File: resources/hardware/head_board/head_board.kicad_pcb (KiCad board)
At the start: 2 copper layers, 66 x 61 mm, 18 parts, among them IC1 ATMEGA328P-P, P1 SERIAL/RST, P2 PI_CONN, P3 REED, P4 PR, P5 CAM_LEDS, P6 STEPPER, P7 PR_LED, P8 FDBK_LED, U1 ULN2003

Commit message: added letterbox-setup.py
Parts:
- C1: value CP1 -> 10 uF
- R1: value R -> 56 Ohm
- R2: value R -> 10 kOhm
- R5, R6: value R -> 100 Ohm
- moved C1 1.65 mm to (149.5, 153.0)
- moved R2 1.27 mm to (163.5, 153.5)
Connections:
- IC1 pad 2: /PIRX -> /PITX
- IC1 pad 3: /PITX -> /PIRX
- P1 pad 2: /PIRX -> /PITX
- P1 pad 3: /PITX -> /PIRX
- R2 pad 2: Net-(C1-Pad2) -> /RST
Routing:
- net /RST: track 8.15 -> 15.5 mm
- net Net-(C1-Pad2): track 11.1 -> 5.62 mm
- net /PITX: track 140.0 -> 144.4 mm, vias 3 -> 1
- net /PIRX: track 139.7 -> 138.7 mm, vias 1 -> 3
- net +3V3: track 95.7 -> 96.5 mm

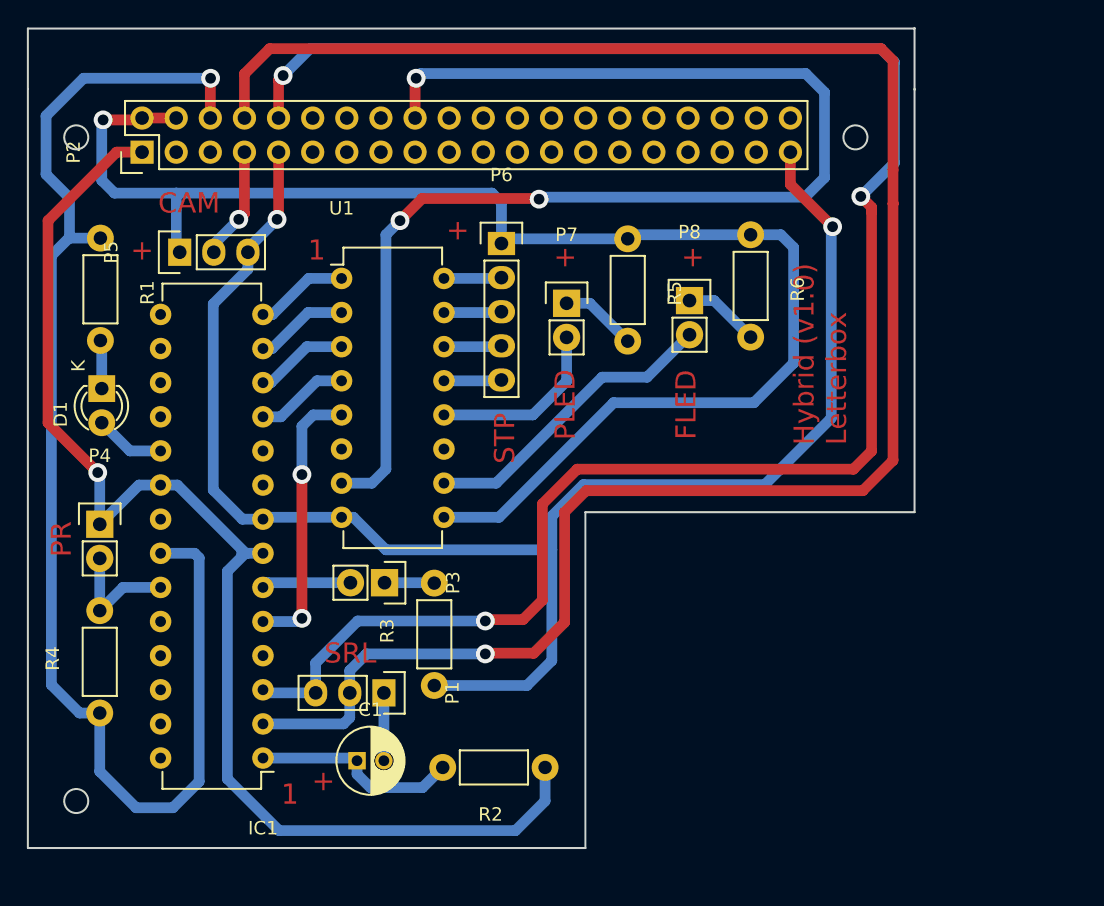
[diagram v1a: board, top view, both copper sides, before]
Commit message: added stepper board
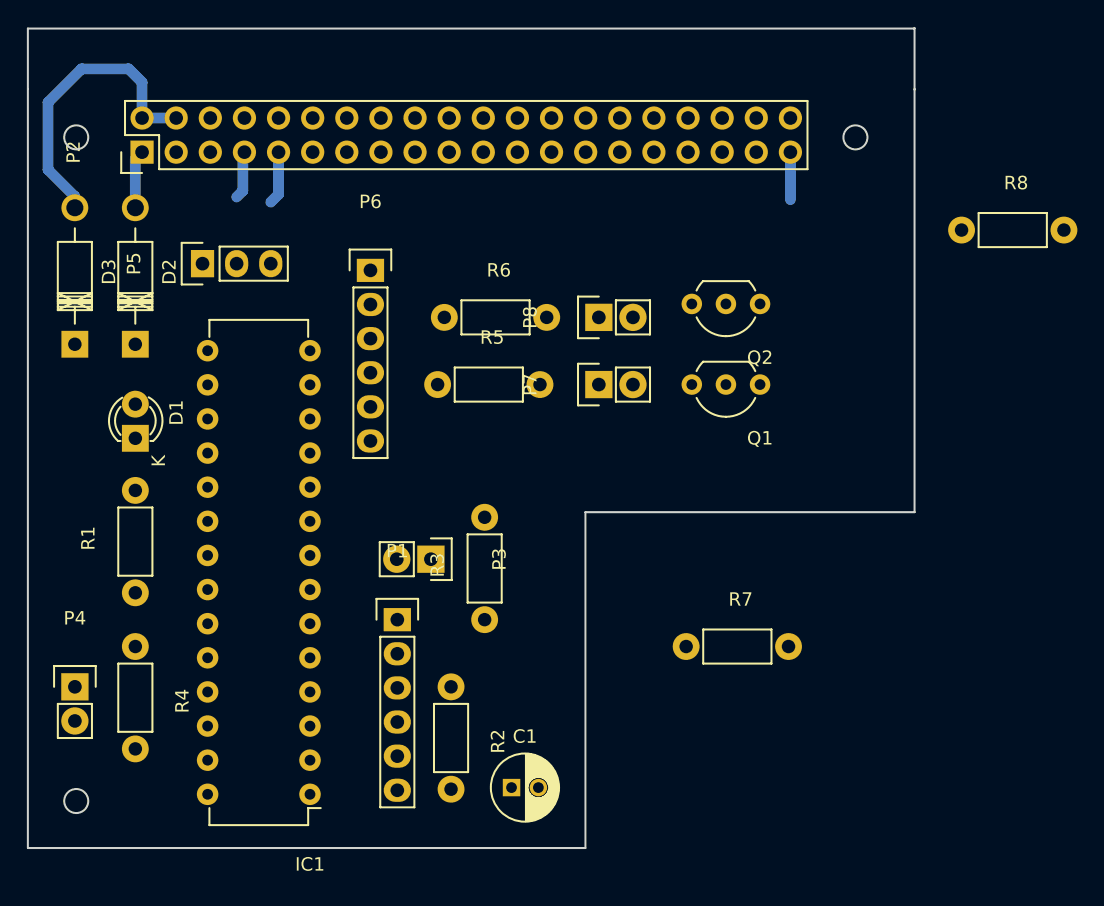
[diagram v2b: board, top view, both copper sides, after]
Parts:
- removed U1: ULN2003, Housings_DIP:DIP-16_W7.62mm
- added D2: D, Diodes_ThroughHole:Diode_DO-41_SOD81_Horizontal_RM10, F.Cu at (133.0, 122.0)
- added D3: D, Diodes_ThroughHole:Diode_DO-41_SOD81_Horizontal_RM10, F.Cu at (128.5, 122.0)
- added Q1: BC547, TO_SOT_Packages_THT:TO-92_Inline_Wide, F.Cu at (179.5, 125.0)
- added Q2: BC547, TO_SOT_Packages_THT:TO-92_Inline_Wide, F.Cu at (179.5, 119.0)
- added R7: 330 Ohm, Resistors_ThroughHole:Resistor_Horizontal_RM7mm, F.Cu at (174.0, 144.5)
- added R8: 330 Ohm, Resistors_ThroughHole:Resistor_Horizontal_RM7mm, F.Cu at (194.5, 113.5)
- P1: value SERIAL/RST -> SERIAL; footprint Pin_Headers:Pin_Header_Straight_1x03 -> Pin_Headers:Pin_Header_Straight_1x06
- P6: footprint Pin_Headers:Pin_Header_Straight_1x05 -> Pin_Headers:Pin_Header_Straight_1x06
- moved R1 26.5 mm to (133.0, 140.5), turned to 90 degrees
- moved R6 23.6 mm to (156.0, 120.0), turned to 0 degrees
- moved R5 17.8 mm to (155.5, 125.0), turned to 0 degrees
- moved P4 12.2 mm to (128.5, 147.5)
- moved C1 11.7 mm to (161.0, 155.0)
- moved P6 9.95 mm to (150.5, 116.5)
- moved R2 9.22 mm to (156.5, 147.5), turned to 270 degrees
- moved P8 6.86 mm to (167.5, 120.0), turned to 90 degrees
- moved P7 6.51 mm to (167.5, 125.0), turned to 90 degrees
- moved R3 6.17 mm to (159.0, 142.5)
- moved R4 5.61 mm to (133.0, 144.5), turned to 270 degrees
- moved P1 5.54 mm to (152.5, 142.5), turned to 0 degrees
- moved D1 4.47 mm to (133.0, 129.0), turned to 90 degrees
- moved IC1 4.42 mm to (146.0, 155.5)
- moved P3 3.87 mm to (155.0, 138.0)
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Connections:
- C1 pad 2: Net-(C1-Pad2) -> /DTR
- P1 pad 1: Net-(C1-Pad2) -> GND
- P1 pad 2: /PITX -> (no net)
- P1 pad 3: /PIRX -> +3V3
- P2 pad 1: +3V3 -> Net-(D2-Pad2)
- P2 pad 2: +5V -> Net-(D3-Pad2)
- P2 pad 4: +5V -> Net-(D3-Pad2)
- P6 pad 2: Net-(P6-Pad2) -> GND
- P6 pad 3: Net-(P6-Pad3) -> /MOT4
- P6 pad 4: Net-(P6-Pad4) -> /MOT3
- P6 pad 5: Net-(P6-Pad5) -> /MOT2
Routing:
- net GND: track 219.7 -> 7.50 mm, vias 3 -> 0
- net /PITX: track 144.4 -> 0.00 mm, vias 1 -> 0
- net /PIRX: track 138.7 -> 0.00 mm, vias 3 -> 0
- net +5V: track 109.8 -> 0.00 mm, vias 1 -> 0
- net +3V3: track 96.5 -> 0.00 mm, vias 1 -> 0
- net /FDBK: track 96.1 -> 0.00 mm, vias 3 -> 0
- net Net-(P8-Pad2): track 22.9 -> 0.00 mm
- net Net-(D3-Pad2): track 0.00 -> 22.3 mm
- net /PRLED: track 20.6 -> 0.00 mm, vias 2 -> 0
- net /RST: track 15.5 -> 0.00 mm
- net Net-(P7-Pad2): track 13.4 -> 0.00 mm
- net /PR: track 9.14 -> 0.00 mm
- net /MOT4: track 6.96 -> 0.00 mm
- net /MOT1: track 6.96 -> 0.00 mm
- net /MOT3: track 6.96 -> 0.00 mm
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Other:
- board text removed: "+"
- board text removed: "1"
- board text removed: "CAM"
- board text removed: "FLED"
- board text removed: "Hybrid (v1.0) Letterbox"
- board text removed: "PLED"
- board text removed: "PR"
- board text removed: "SRL"
- board text removed: "STP"

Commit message: finished new headboard pcbs
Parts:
- moved R3 27.7 mm to (156.2, 114.9), turned to 270 degrees
- moved R7 21.2 mm to (162.1, 127.0)
- moved D3 21.0 mm to (146.8, 111.8), turned to 180 degrees
- moved R8 14.8 mm to (179.8, 111.3), turned to 270 degrees
- moved R5 12.3 mm to (162.3, 114.8), turned to 270 degrees
- moved R6 11.4 mm to (166.1, 114.8), turned to 270 degrees
- moved P3 11.1 mm to (156.2, 127.0), turned to 0 degrees
- moved Q2 10.7 mm to (169.9, 114.2), turned to 0 degrees
- moved C1 10.1 mm to (150.9, 154.9), turned to 90 degrees
- moved P5 5.80 mm to (143.8, 115.3), turned to 270 degrees
- moved R2 4.16 mm to (160.0, 145.3)
- moved P1 4.15 mm to (156.0, 140.2)
- moved D2 3.63 mm to (129.5, 120.9)
- moved P7 3.62 mm to (170.6, 123.1)
- moved Q1 3.54 mm to (182.4, 122.9)
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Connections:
- P2 pad 17: +3V3 -> (no net)
- P2 pad 18: /FDBK -> (no net)
- P2 pad 31: (no net) -> /FDBK
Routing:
- net GND: track 7.50 -> 251.4 mm, vias 0 -> 3
- net /PITX: track 0.00 -> 140.8 mm, vias 0 -> 1
- net /PIRX: track 0.00 -> 138.6 mm, vias 0 -> 1
- net +3V3: track 0.00 -> 69.6 mm, vias 0 -> 2
- net /PRLED: track 0.00 -> 39.7 mm
- net +5V: track 0.00 -> 32.1 mm
- net /PR: track 0.00 -> 20.0 mm
- net /REED: track 0.00 -> 17.6 mm
- net /RST: track 0.00 -> 16.9 mm
- net Net-(Q2-Pad2): track 0.00 -> 15.1 mm
- net /FDBK: track 0.00 -> 11.1 mm
- net Net-(P7-Pad1): track 0.00 -> 11.0 mm
- net Net-(D3-Pad2): track 22.3 -> 33.1 mm
- net /LED: track 0.00 -> 9.63 mm
- net Net-(P8-Pad1): track 0.00 -> 6.02 mm
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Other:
- net class Default: via_dia 1.4 -> 1.7
- board text added: "FDBK"
- board text added: "G"
- board text added: "PR"
- board text added: "PRL"
- board text added: "REED"
- board text added: "SRL"

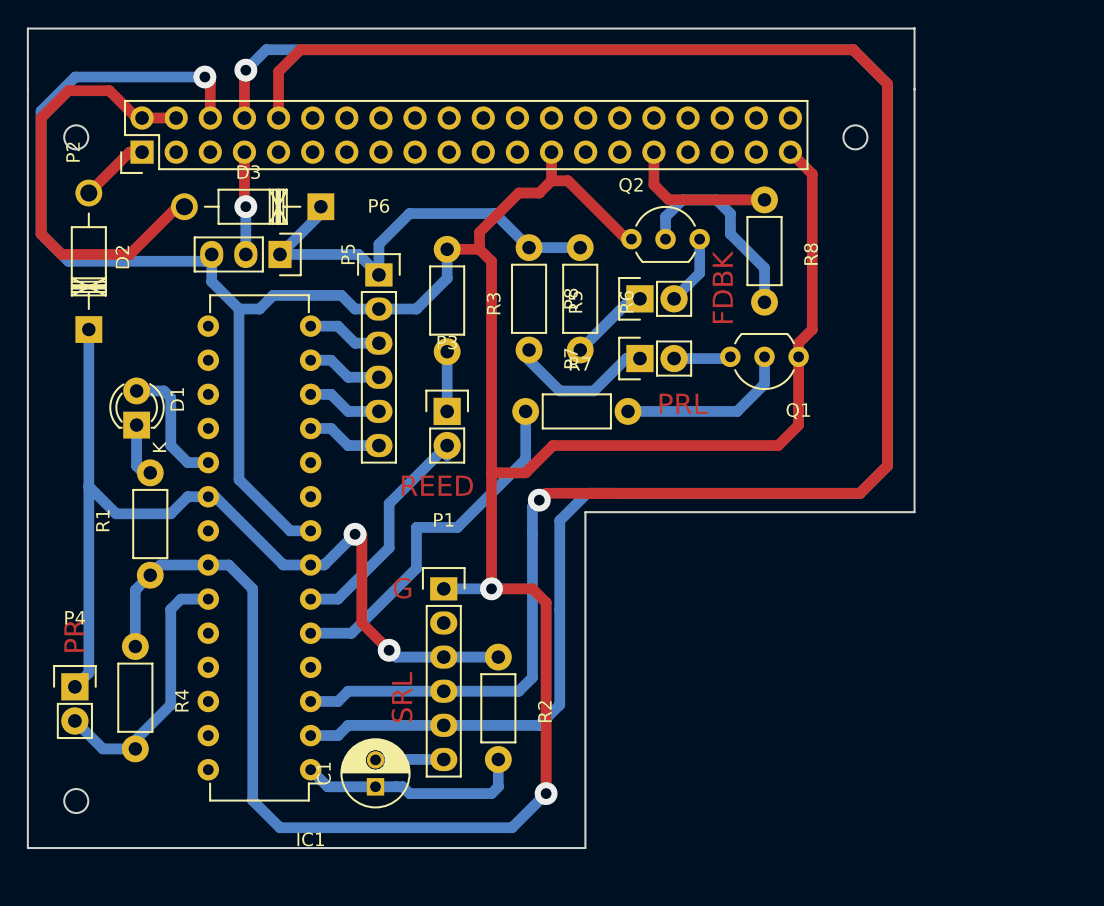
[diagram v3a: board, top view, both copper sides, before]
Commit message: deleted old headboard, modified new
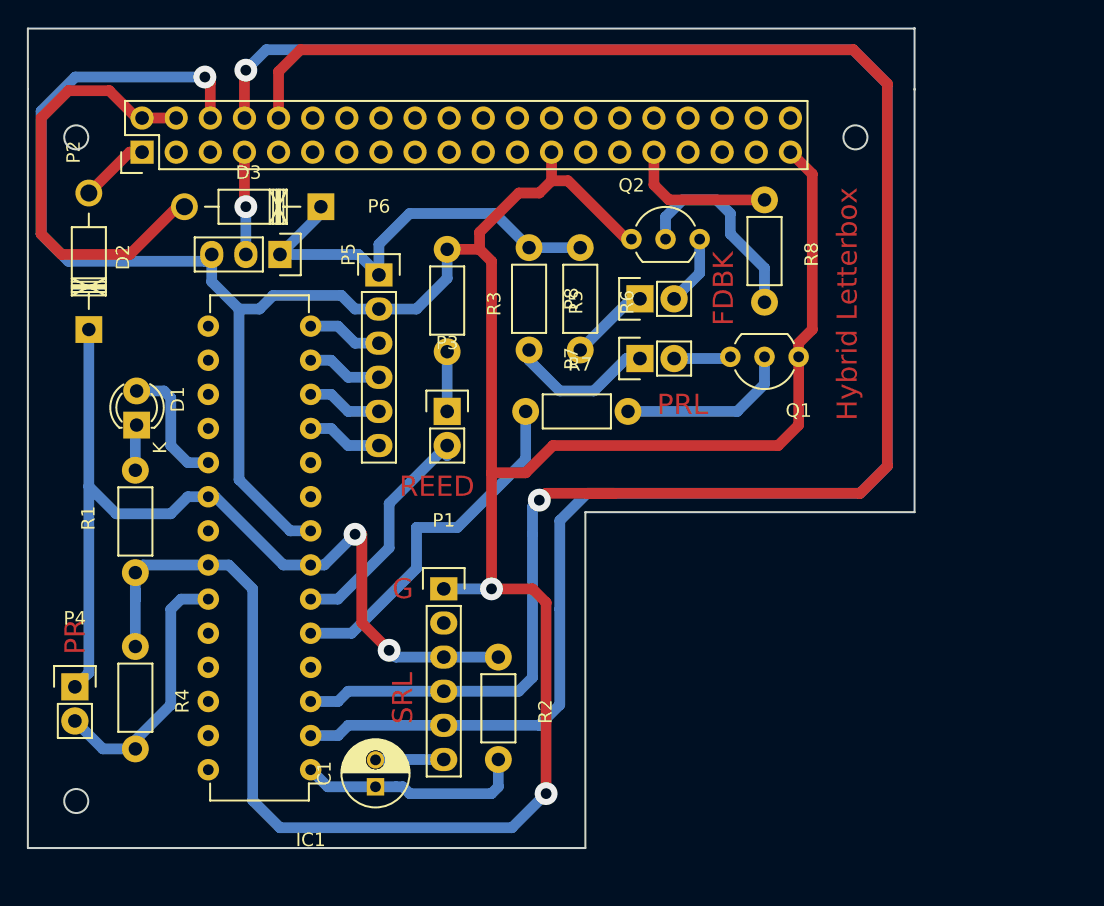
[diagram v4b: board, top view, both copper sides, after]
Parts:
- moved R1 1.13 mm to (133.0, 139.0)
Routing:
- net GND: track 251.4 -> 252.9 mm
- net Net-(D1-Pad1): track 4.27 -> 3.40 mm
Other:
- board text added: "Hybrid Letterbox"
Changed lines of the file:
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@@
-(kicad_pcb (version 4) (host pcbnew 4.0.2-stable)
+(kicad_pcb (version 4) (host pcbnew 4.0.1-stable)
   (general
     (links 56)
@@
     (area 124.924999 98.374999 191.075001 159.575001)
     (thickness 1.6)
-    (drawings 23)
+    (drawings 24)
     (tracks 214)
     (zones 0)
@@
   )
   (module Resistors_ThroughHole:Resistor_Horizontal_RM7mm (layer F.Cu)
-    (at 134.112 139.192 90)
+    (at 133 139 90)
     (descr "Resistor, Axial,  RM 7.62mm, 1/3W,")
     (tags "Resistor Axial RM 7.62mm 1/3W R3")
@@
     (pad 2 thru_hole circle (at 7.62 0 270) (size 1.99898 1.99898) (drill 1.00076) (layers *.Cu *.SilkS *.Mask)
       (net 23 "Net-(Q2-Pad2)"))
+  )
+  (gr_text "Hybrid Letterbox" (at 186 119 90) (layer F.Cu)
+    (effects (font (size 1.5 1.5) (thickness 0.3)))
   )
   (gr_text FDBK (at 176.784 117.856 90) (layer F.Cu)
@@
   (segment (start 150.876 154.94) (end 147.32 154.94) (width 0.8) (layer B.Cu) (net 1))
   (segment (start 147.32 154.94) (end 146.05 153.67) (width 0.8) (layer B.Cu) (net 1))
-  (segment (start 134.112 131.572) (end 133.604 131.572) (width 0.8) (layer B.Cu) (net 2))
-  (segment (start 133.604 131.572) (end 133.096 131.064) (width 0.8) (layer B.Cu) (net 2))
-  (segment (start 133.096 131.064) (end 133.096 128.016) (width 0.8) (layer B.Cu) (net 2))
+  (segment (start 133 131.38) (end 133 128.112) (width 0.8) (layer B.Cu) (net 2) (status C00000))
+  (segment (start 133 128.112) (end 133.096 128.016) (width 0.8) (layer B.Cu) (net 2) (status C00000))
   (segment (start 136.906 130.81) (end 138.43 130.81) (width 0.8) (layer B.Cu) (net 3))
   (segment (start 135.636 129.54) (end 136.906 130.81) (width 0.8) (layer B.Cu) (net 3))
@@
   (segment (start 131.572 134.62) (end 135.636 134.62) (width 0.8) (layer B.Cu) (net 7))
   (segment (start 129.53746 132.58546) (end 131.572 134.62) (width 0.8) (layer B.Cu) (net 7))
+  (segment (start 133 141) (end 133 139) (width 0.8) (layer B.Cu) (net 8) (status 800000))
+  (segment (start 133 139) (end 133.57 138.43) (width 0.8) (layer B.Cu) (net 8) (status C00000))
+  (segment (start 133.57 138.43) (end 138.43 138.43) (width 0.8) (layer B.Cu) (net 8) (status C00000))
   (segment (start 159.512 131.572) (end 162.052 131.572) (width 0.8) (layer F.Cu) (net 8))
   (segment (start 182.372 128.016) (end 182.372 122.936) (width 0.8) (layer F.Cu) (net 8))
@@
   (segment (start 143.256 118.364) (end 148.336 118.364) (width 0.8) (layer B.Cu) (net 8))
   (segment (start 142.24 119.38) (end 143.256 118.364) (width 0.8) (layer B.Cu) (net 8))
-  (segment (start 133 144.5) (end 133 140.304) (width 0.8) (layer B.Cu) (net 8))
-  (segment (start 133 140.304) (end 134.112 139.192) (width 0.8) (layer B.Cu) (net 8))
-  (segment (start 138.43 138.43) (end 134.874 138.43) (width 0.8) (layer B.Cu) (net 8))
-  (segment (start 134.874 138.43) (end 134.112 139.192) (width 0.8) (layer B.Cu) (net 8))
+  (segment (start 133 144.5) (end 133 141) (width 0.8) (layer B.Cu) (net 8))
+  (segment (start 133 141) (end 133 140.304) (width 0.8) (layer B.Cu) (net 8))
   (segment (start 138.684 115.316) (end 138.684 117.348) (width 0.8) (layer B.Cu) (net 8))
   (segment (start 144.526 135.89) (end 146.05 135.89) (width 0.8) (layer B.Cu) (net 8))
